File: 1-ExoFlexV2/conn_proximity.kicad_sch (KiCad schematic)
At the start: 40 parts, among them J30 1751099, J31 1751099, J32 1751099, J33 1751099, J34 1751112, J35 1751112, J36 1751112, J37 1751112, J38 200k, J39 200k, J40 200k, J41 200k

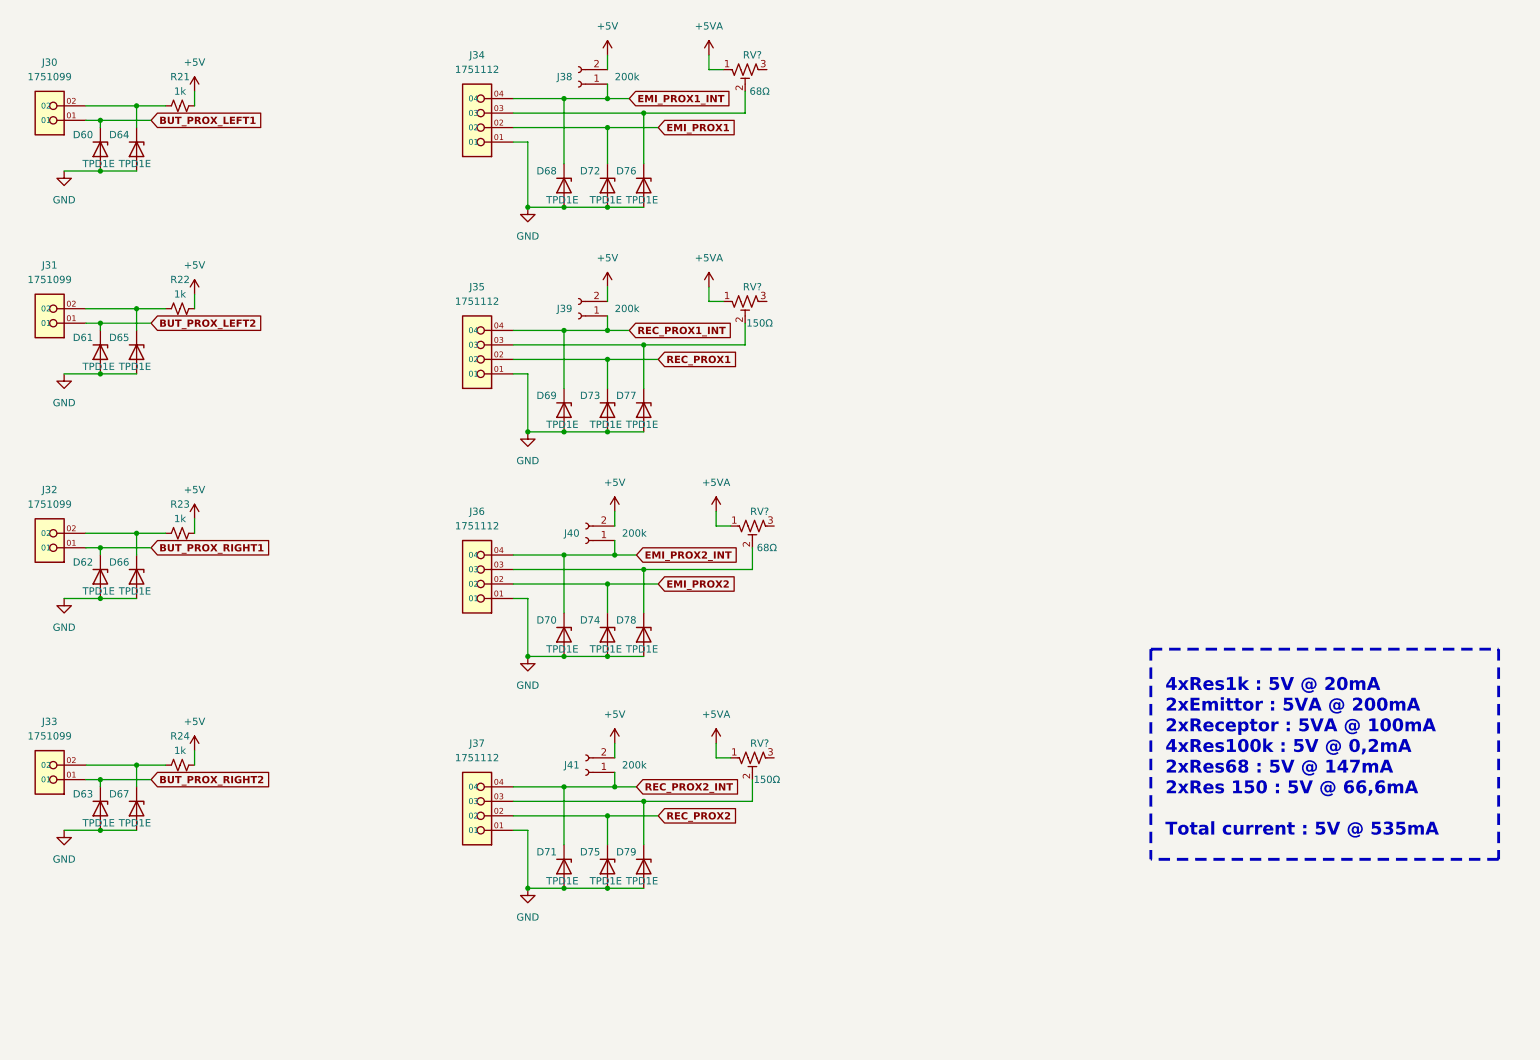
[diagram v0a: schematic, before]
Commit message: Trimmer et jumper
-Changement de symbole de jumper
-Ajout des des trimmer aux endroits nécessaires
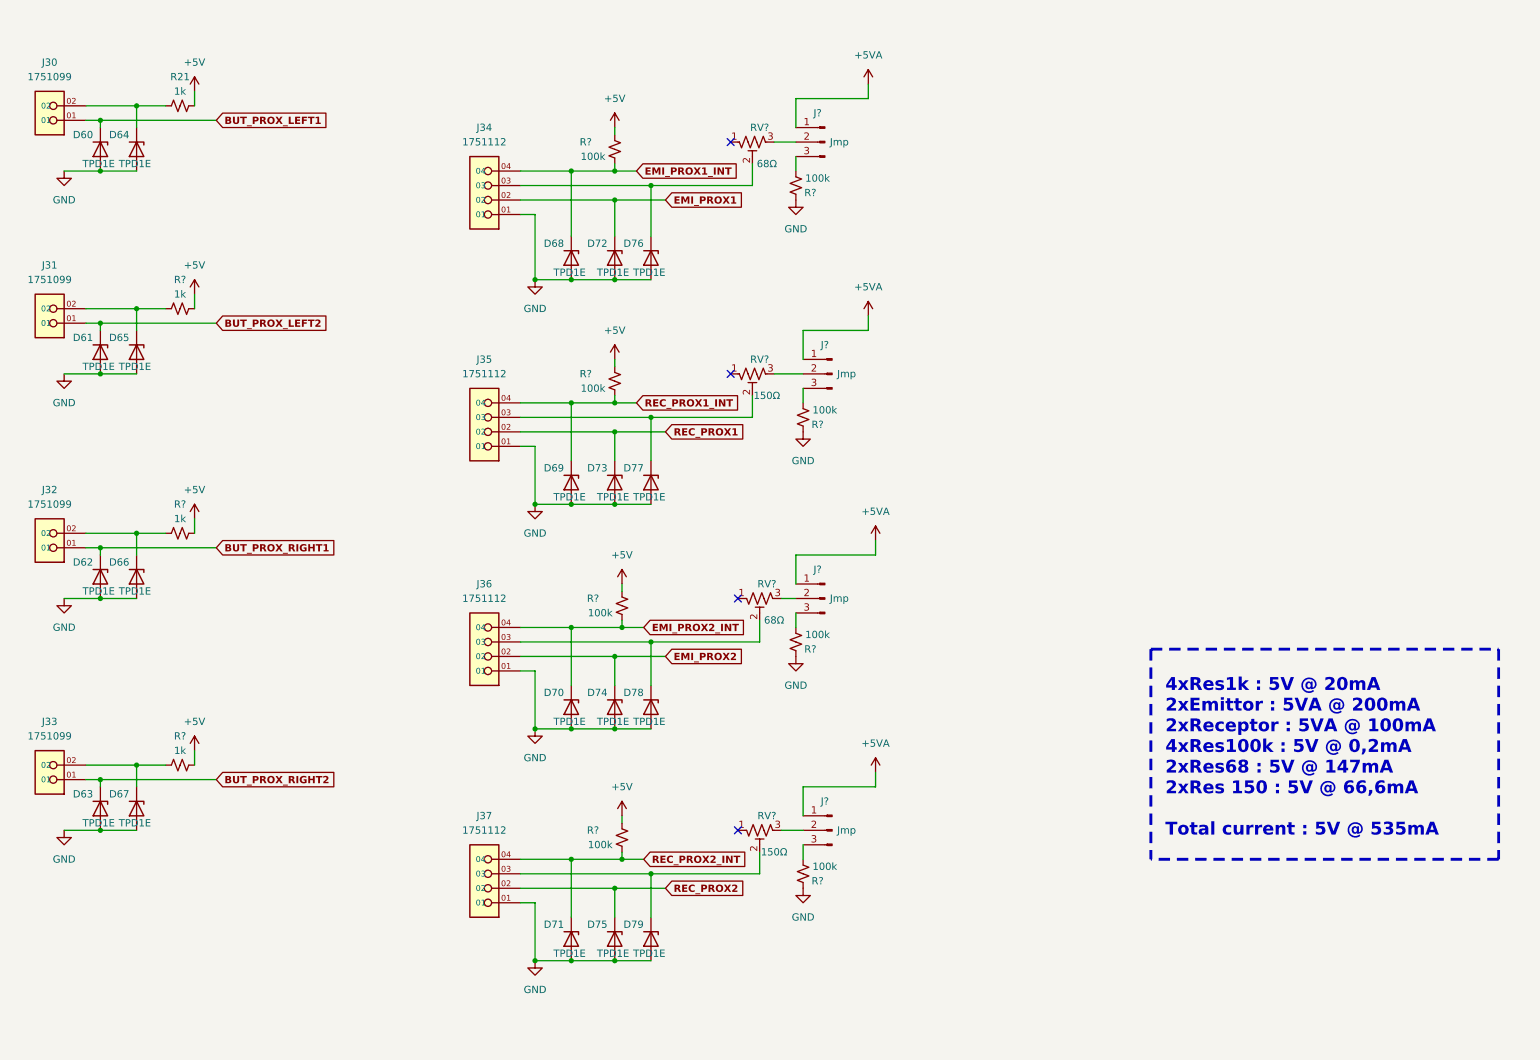
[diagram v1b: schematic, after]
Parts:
- removed J38, J39, J40, J41: 200k, Connector_PinHeader_2.54mm:PinHeader_1x02_P2.54mm_Vertical, symbol Connector:Conn_01x02_Female
- removed R22, R23, R24: 1k, Resistor_SMD:R_0603_1608Metric, symbol Device:R_Small_US
- added J? (x4): Jmp, symbol Connector:Conn_01x03_Male
- added R? (x3): 1k, Resistor_SMD:R_0805_2012Metric, symbol Device:R_Small_US
- added R? (x8): 100k, Resistor_SMD:R_0805_2012Metric, symbol Device:R_Small_US
- R21: footprint Resistor_SMD:R_0603_1608Metric -> Resistor_SMD:R_0805_2012Metric
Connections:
- net +5V: now also R?.1, R?.1, R?.1, R?.1, R?.2, R?.2, R?.2
- net +5VA: now also J?.1 (Pin_1), J?.1 (Pin_1), J?.1 (Pin_1), J?.1 (Pin_1); no longer RV?.1, RV?.1, RV?.1, RV?.1
- net EMI_PROX1_INT: now also R?.2
- net EMI_PROX2_INT: now also R?.2
- net GND: now also R?.2, R?.2, R?.2, R?.2
- net REC_PROX1_INT: now also R?.2
- net REC_PROX2_INT: now also R?.2
- net at RV?.3: now also J?.2 (Pin_2) (x4)
- net at D66.1 (K), J32.02: now also R?.1
- net at D65.1 (K), J31.02: now also R?.1
- net at D67.1 (K), J33.02: now also R?.1
- new net: J?.3 (Pin_3), R?.1 (x4)
- no-connect marks 0 -> 4
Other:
- moved on the sheet: D68, D69, D70, D71, D72, D73, D74, D75, D76, D77, D78, D79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

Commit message: Test points et notes
- Ajout de tous les tests point nécessaires
-  Ajoute des sections de notes dans chaque page
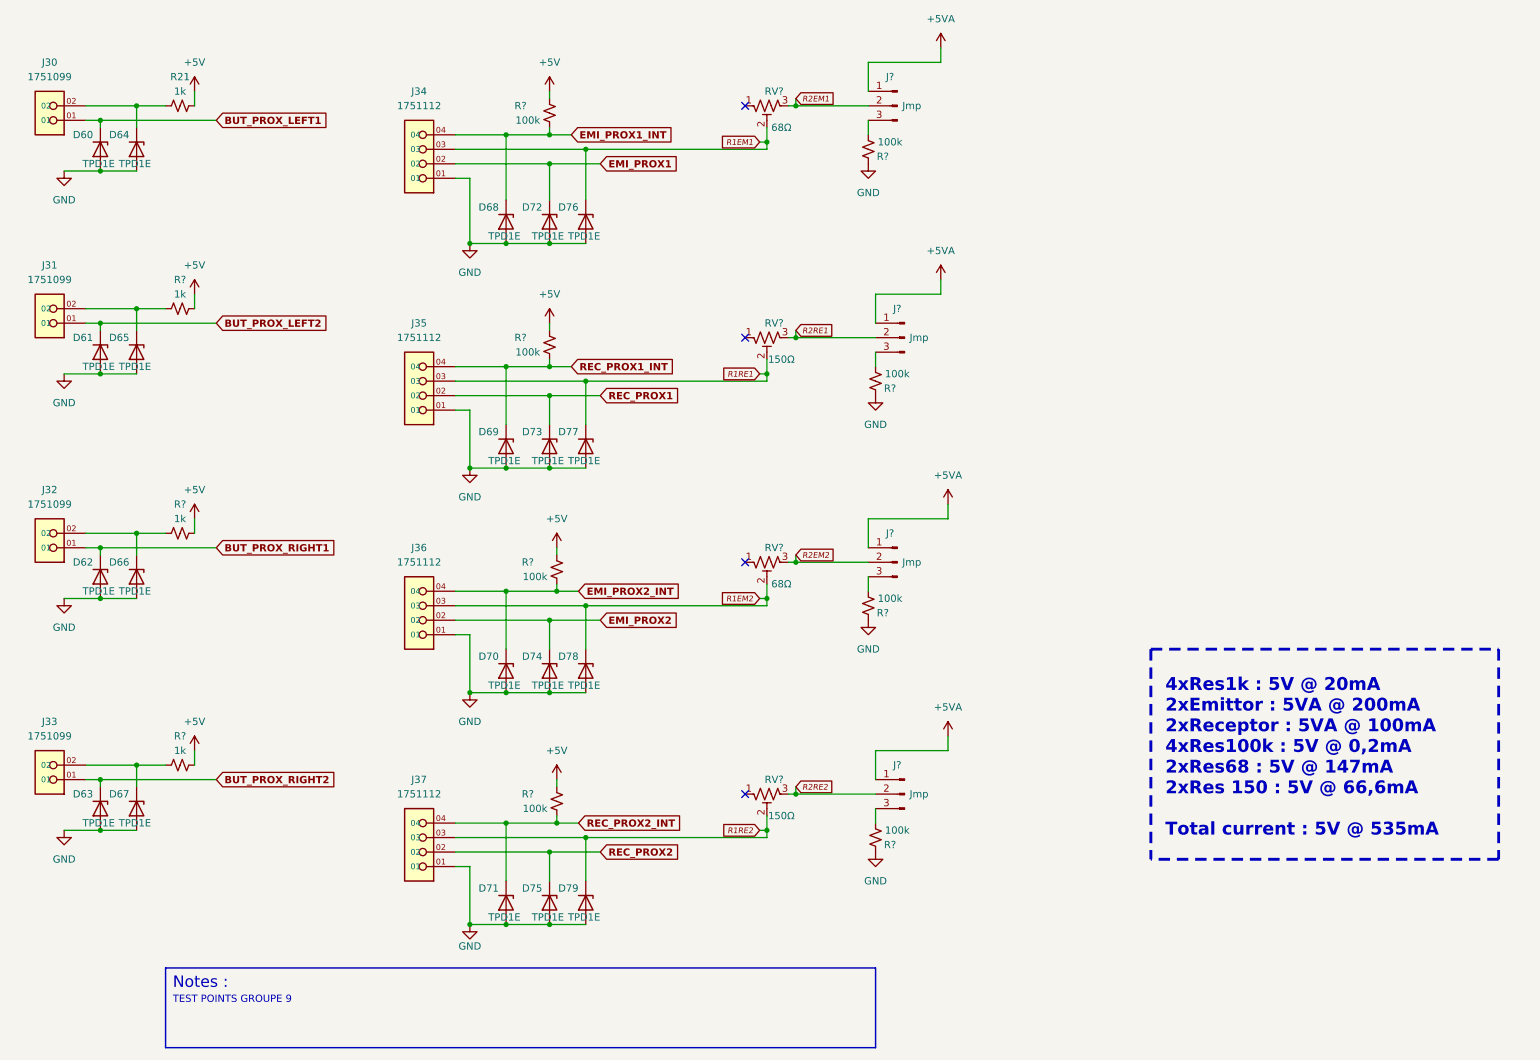
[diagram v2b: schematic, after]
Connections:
- net R1EM2: now reaches D78.1 (K), J36.03, RV?.2
- net R2EM2: now reaches J?.2 (Pin_2), RV?.3
- net R1RE2: now reaches D79.1 (K), J37.03, RV?.2
- net R1RE1: now reaches D77.1 (K), J35.03, RV?.2
- net R2RE1: now reaches J?.2 (Pin_2), RV?.3
- net R2RE2: now reaches J?.2 (Pin_2), RV?.3
- net R1EM1: now reaches D76.1 (K), J34.03, RV?.2
- net R2EM1: now reaches J?.2 (Pin_2), RV?.3
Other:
- note added: "Notes :"
- note added: "TEST POINTS GROUPE 9"
- moved on the sheet: D68, D69, D70, D71, D72, D73, D74, D75, D76, D77, D78, D79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

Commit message: Schématisation terminée
- Schéma terminé
- Passage vers le PCB
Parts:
- removed R? (x4): 100k, Resistor_SMD:R_0805_2012Metric, symbol Device:R_Small_US
- D59: renamed from D60; value TPD1E -> TVS; DESCRIPTION (none) -> TVS DIODE 5.5VWM 14VC 2X1SON; MANUFACTURER (none) -> Texas Instruments; PACKAGE (none) -> 0402 (1006 Metric); PART NUMBER (none) -> TPD1E05U06DPYR; TYPE (none) -> SMD
- D60: renamed from D61; value TPD1E -> TVS; DESCRIPTION (none) -> TVS DIODE 5.5VWM 14VC 2X1SON; MANUFACTURER (none) -> Texas Instruments; PACKAGE (none) -> 0402 (1006 Metric); PART NUMBER (none) -> TPD1E05U06DPYR; TYPE (none) -> SMD
- D61: renamed from D62; value TPD1E -> TVS; DESCRIPTION (none) -> TVS DIODE 5.5VWM 14VC 2X1SON; MANUFACTURER (none) -> Texas Instruments; PACKAGE (none) -> 0402 (1006 Metric); PART NUMBER (none) -> TPD1E05U06DPYR; TYPE (none) -> SMD
- D62: renamed from D63; value TPD1E -> TVS; DESCRIPTION (none) -> TVS DIODE 5.5VWM 14VC 2X1SON; MANUFACTURER (none) -> Texas Instruments; PACKAGE (none) -> 0402 (1006 Metric); PART NUMBER (none) -> TPD1E05U06DPYR; TYPE (none) -> SMD
- D63: renamed from D64; value TPD1E -> TVS; DESCRIPTION (none) -> TVS DIODE 5.5VWM 14VC 2X1SON; MANUFACTURER (none) -> Texas Instruments; PACKAGE (none) -> 0402 (1006 Metric); PART NUMBER (none) -> TPD1E05U06DPYR; TYPE (none) -> SMD
- D64: renamed from D65; value TPD1E -> TVS; DESCRIPTION (none) -> TVS DIODE 5.5VWM 14VC 2X1SON; MANUFACTURER (none) -> Texas Instruments; PACKAGE (none) -> 0402 (1006 Metric); PART NUMBER (none) -> TPD1E05U06DPYR; TYPE (none) -> SMD
- D65: renamed from D66; value TPD1E -> TVS; DESCRIPTION (none) -> TVS DIODE 5.5VWM 14VC 2X1SON; MANUFACTURER (none) -> Texas Instruments; PACKAGE (none) -> 0402 (1006 Metric); PART NUMBER (none) -> TPD1E05U06DPYR; TYPE (none) -> SMD
- D66: renamed from D67; value TPD1E -> TVS; DESCRIPTION (none) -> TVS DIODE 5.5VWM 14VC 2X1SON; MANUFACTURER (none) -> Texas Instruments; PACKAGE (none) -> 0402 (1006 Metric); PART NUMBER (none) -> TPD1E05U06DPYR; TYPE (none) -> SMD
- D67: renamed from D68; value TPD1E -> TVS; DESCRIPTION (none) -> TVS DIODE 5.5VWM 14VC 2X1SON; MANUFACTURER (none) -> Texas Instruments; PACKAGE (none) -> 0402 (1006 Metric); PART NUMBER (none) -> TPD1E05U06DPYR; TYPE (none) -> SMD
- D68: renamed from D69; value TPD1E -> TVS; DESCRIPTION (none) -> TVS DIODE 5.5VWM 14VC 2X1SON; MANUFACTURER (none) -> Texas Instruments; PACKAGE (none) -> 0402 (1006 Metric); PART NUMBER (none) -> TPD1E05U06DPYR; TYPE (none) -> SMD
- D69: renamed from D70; value TPD1E -> TVS; DESCRIPTION (none) -> TVS DIODE 5.5VWM 14VC 2X1SON; MANUFACTURER (none) -> Texas Instruments; PACKAGE (none) -> 0402 (1006 Metric); PART NUMBER (none) -> TPD1E05U06DPYR; TYPE (none) -> SMD
- D70: renamed from D71; value TPD1E -> TVS; DESCRIPTION (none) -> TVS DIODE 5.5VWM 14VC 2X1SON; MANUFACTURER (none) -> Texas Instruments; PACKAGE (none) -> 0402 (1006 Metric); PART NUMBER (none) -> TPD1E05U06DPYR; TYPE (none) -> SMD
- D71: renamed from D72; value TPD1E -> TVS; DESCRIPTION (none) -> TVS DIODE 5.5VWM 14VC 2X1SON; MANUFACTURER (none) -> Texas Instruments; PACKAGE (none) -> 0402 (1006 Metric); PART NUMBER (none) -> TPD1E05U06DPYR; TYPE (none) -> SMD
- D72: renamed from D73; value TPD1E -> TVS; DESCRIPTION (none) -> TVS DIODE 5.5VWM 14VC 2X1SON; MANUFACTURER (none) -> Texas Instruments; PACKAGE (none) -> 0402 (1006 Metric); PART NUMBER (none) -> TPD1E05U06DPYR; TYPE (none) -> SMD
- D73: renamed from D74; value TPD1E -> TVS; DESCRIPTION (none) -> TVS DIODE 5.5VWM 14VC 2X1SON; MANUFACTURER (none) -> Texas Instruments; PACKAGE (none) -> 0402 (1006 Metric); PART NUMBER (none) -> TPD1E05U06DPYR; TYPE (none) -> SMD
- D74: renamed from D75; value TPD1E -> TVS; DESCRIPTION (none) -> TVS DIODE 5.5VWM 14VC 2X1SON; MANUFACTURER (none) -> Texas Instruments; PACKAGE (none) -> 0402 (1006 Metric); PART NUMBER (none) -> TPD1E05U06DPYR; TYPE (none) -> SMD
- D75: renamed from D76; value TPD1E -> TVS; DESCRIPTION (none) -> TVS DIODE 5.5VWM 14VC 2X1SON; MANUFACTURER (none) -> Texas Instruments; PACKAGE (none) -> 0402 (1006 Metric); PART NUMBER (none) -> TPD1E05U06DPYR; TYPE (none) -> SMD
- D76: renamed from D77; value TPD1E -> TVS; DESCRIPTION (none) -> TVS DIODE 5.5VWM 14VC 2X1SON; MANUFACTURER (none) -> Texas Instruments; PACKAGE (none) -> 0402 (1006 Metric); PART NUMBER (none) -> TPD1E05U06DPYR; TYPE (none) -> SMD
- D77: renamed from D78; value TPD1E -> TVS; DESCRIPTION (none) -> TVS DIODE 5.5VWM 14VC 2X1SON; MANUFACTURER (none) -> Texas Instruments; PACKAGE (none) -> 0402 (1006 Metric); PART NUMBER (none) -> TPD1E05U06DPYR; TYPE (none) -> SMD
- D78: renamed from D79; value TPD1E -> TVS; DESCRIPTION (none) -> TVS DIODE 5.5VWM 14VC 2X1SON; MANUFACTURER (none) -> Texas Instruments; PACKAGE (none) -> 0402 (1006 Metric); PART NUMBER (none) -> TPD1E05U06DPYR; TYPE (none) -> SMD
- J35: renamed from J30; value 1751099 -> 2; DESCRIPTION (none) -> 2 Position Wire to Board Terminal Block 55° (125°) Angle wi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; PACKAGE (none) -> 2 POS 0.100" (2.54mm); PART NUMBER (none) -> 1751099; TYPE (none) -> Through Hole
- J36: renamed from J31; value 1751099 -> 2; DESCRIPTION (none) -> 2 Position Wire to Board Terminal Block 55° (125°) Angle wi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; PACKAGE (none) -> 2 POS 0.100" (2.54mm); PART NUMBER (none) -> 1751099; TYPE (none) -> Through Hole
- J37: renamed from J32; value 1751099 -> 2; DESCRIPTION (none) -> 2 Position Wire to Board Terminal Block 55° (125°) Angle wi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; PACKAGE (none) -> 2 POS 0.100" (2.54mm); PART NUMBER (none) -> 1751099; TYPE (none) -> Through Hole
- J38: renamed from J33; value 1751099 -> 2; DESCRIPTION (none) -> 2 Position Wire to Board Terminal Block 55° (125°) Angle wi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; PACKAGE (none) -> 2 POS 0.100" (2.54mm); PART NUMBER (none) -> 1751099; TYPE (none) -> Through Hole
- J39: renamed from J34; value 1751112 -> 4; DESCRIPTION (none) -> 4 Position Wire to Board Terminal Block 55° (125°) Angle wi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; PACKAGE (none) -> 4 POS 0.100" (2.54mm); PART NUMBER (none) -> 1751112; TYPE (none) -> Through Hole
- J40: renamed from J35; value 1751112 -> 4; DESCRIPTION (none) -> 4 Position Wire to Board Terminal Block 55° (125°) Angle wi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; PACKAGE (none) -> 4 POS 0.100" (2.54mm); PART NUMBER (none) -> 1751112; TYPE (none) -> Through Hole
- J41: renamed from J36; value 1751112 -> 4; DESCRIPTION (none) -> 4 Position Wire to Board Terminal Block 55° (125°) Angle wi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; PACKAGE (none) -> 4 POS 0.100" (2.54mm); PART NUMBER (none) -> 1751112; TYPE (none) -> Through Hole
- J42: renamed from J37; value 1751112 -> 4; DESCRIPTION (none) -> 4 Position Wire to Board Terminal Block 55° (125°) Angle wi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; PACKAGE (none) -> 4 POS 0.100" (2.54mm); PART NUMBER (none) -> 1751112; TYPE (none) -> Through Hole
- J43, J44, J45, J46: renamed from J?; value Jmp -> Jumper; footprint (none) -> Connector_PinSocket_2.54mm:PinSocket_1x03_P2.54mm_Vertical; DESCRIPTION (none) -> CONN HEADER VERT 3POS 2.54MM; MANUFACTURER (none) -> Würth Elektronik; PACKAGE (none) -> Square 0.100" (2.54mm); PART NUMBER (none) -> 61300311121; TYPE (none) -> Through Hole
- R21: value 1k -> 1k 1% 1/10W; footprint Resistor_SMD:R_0805_2012Metric -> Resistor_SMD:R_0402_1005Metric; DESCRIPTION (none) -> 1 kOhms ±1% 0.1W, 1/10W Chip Resistor 0402 (1005 Metric) Au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; MANUFACTURER (none) -> Panasonic Electronic Components; PACKAGE (none) -> 0402 (1005 Metric); PART NUMBER (none) -> ERJ-2RKF1001X; TYPE (none) -> SMD
- R22, R23, R24: renamed from R?; value 1k -> 1k 1% 1/10W; footprint Resistor_SMD:R_0805_2012Metric -> Resistor_SMD:R_0402_1005Metric; DESCRIPTION (none) -> 1 kOhms ±1% 0.1W, 1/10W Chip Resistor 0402 (1005 Metric) Au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; MANUFACTURER (none) -> Panasonic Electronic Components; PACKAGE (none) -> 0402 (1005 Metric); PART NUMBER (none) -> ERJ-2RKF1001X; TYPE (none) -> SMD
- R25, R26, R27, R28: renamed from R?; value 100k -> 100k 5% 1/8W; DESCRIPTION (none) -> 100 kOhms ±5% 0.125W, 1/8W Chip Resistor 0805 (2012 Metric)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; MANUFACTURER (none) -> Panasonic Electronic Components; PACKAGE (none) -> 0805 (2012 Metric); PART NUMBER (none) -> ERJ-6GEYJ104V; TYPE (none) -> SMD
- RV2, RV4: renamed from RV?; value 68Ω -> Trim 1k; DESCRIPTION (none) -> Trimmer 1k 0,5W PC PIN TOP; MANUFACTURER (none) -> Bourns Inc.; PACKAGE (none) -> Rectangular - 0.275" x 0.260" Face; PART NUMBER (none) -> 3362P-1-102LF; TYPE (none) -> Through Hole
- RV3, RV5: renamed from RV?; value 150Ω -> Trim 1k; DESCRIPTION (none) -> Trimmer 1k 0,5W PC PIN TOP; MANUFACTURER (none) -> Bourns Inc.; PACKAGE (none) -> Rectangular - 0.275" x 0.260" Face; PART NUMBER (none) -> 3362P-1-102LF; TYPE (none) -> Through Hole
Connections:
- net GND: now also J43.3 (Pin_3), J44.3 (Pin_3), J45.3 (Pin_3), J46.3 (Pin_3)
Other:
- note added: "150Ω"
- note added: "4xRes1k : 5V @ 20mA 2xEmittor : 5VA @ 200mA 2xReceptor : 5VA @ 100mA 4xRes100k : 5V @ 0,2mA 2xPot68 : 5VA @ 200mA 2xPot150 : 5VA @ 38,46mA Total current : 5V @ 25mA 5VA @ 543mA"
- note added: "68Ω"
- note added: "But Prox L1"
- note added: "But Prox L2"
- note added: "But Prox R1"
- note added: "But Prox R2"
- note added: "Emi Prox 1"
- note added: "Emi Prox 2"
- note added: "Rec Prox 1"
- note added: "Rec Prox 2"
- note removed: "4xRes1k : 5V @ 20mA 2xEmittor : 5VA @ 200mA 2xReceptor : 5VA @ 100mA 4xRes100k : 5V @ 0,2mA 2xRes68 : 5V @ 147mA 2xRes 150 : 5V @ 66,6mA Total current : 5V @ 535mA"

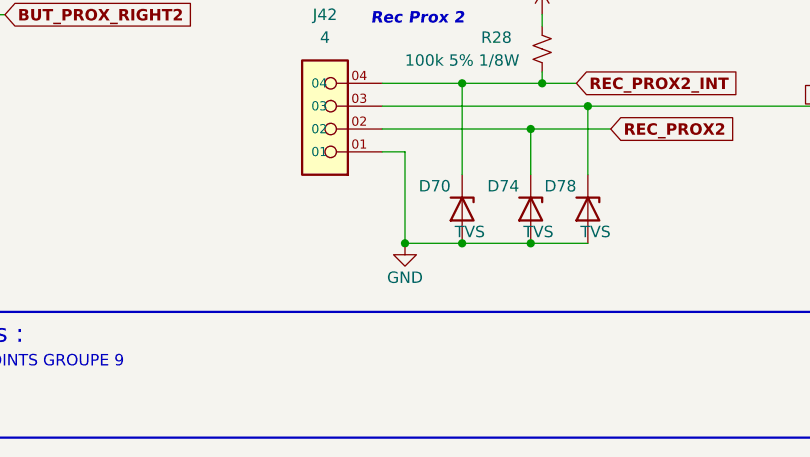
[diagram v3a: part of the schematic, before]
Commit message: Bug NetList
- Ajout de net-tie pour les GND et et les +5V
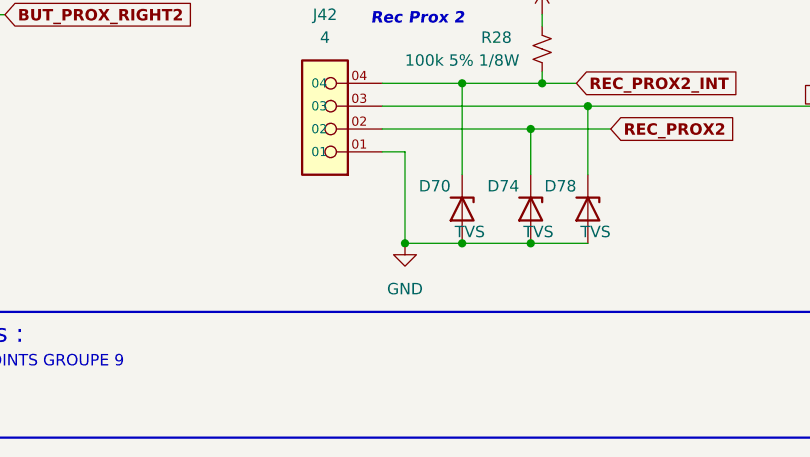
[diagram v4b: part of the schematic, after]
